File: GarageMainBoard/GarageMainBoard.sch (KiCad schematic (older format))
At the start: 33 parts, among them J1 Conn_01x02, J2 Barrel_Jack, J3 Conn_02x13_Odd_Even, J4 Front_Panel_Connector, J5 RJ45, J6 RJ45, Q1 IRLML6344, Q2 IRLML6344, Q3 IRLML6344, U1 AP1117-33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

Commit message: Main PCB start
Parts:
- BZ1: footprint (none) -> Buzzers_Beepers:BUZZER
- C1: footprint (none) -> Capacitors_THT:CP_Radial_D10.0mm_P2.50mm
- C2, C3, C4, C5: footprint (none) -> Capacitors_SMD:C_0805_HandSoldering
- J1: footprint (none) -> Pin_Headers:Pin_Header_Straight_1x02
- J2: footprint (none) -> Connectors:BARREL_JACK
- J3: footprint (none) -> Pin_Headers:Pin_Header_Straight_2x13
- J4: footprint (none) -> Connectors_JST:JST_PH_B8B-PH-K_08x2.00mm_Straight
- J5, J6: footprint (none) -> KevinLibrary:RJ45_LOW_PROFILE_NO_CUT
- Q1, Q2, Q3: footprint (none) -> TO_SOT_Packages_SMD:SOT-23_Handsoldering
- R1, R10, R11, R12, R13, R14, R15, R2, R3, R4, R5, R6, R7, R8, R9: footprint (none) -> Resistors_SMD:R_0805_HandSoldering
- U2, U3: footprint (none) -> KevinLibrary:SLP1616P6
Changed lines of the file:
@@
 LIBS:contrib
 LIBS:valves
-LIBS:KevinsLib
+LIBS:GarageMainBoard-cache
 EELAYER 25 0
 EELAYER END
@@
 F 0 "J5" H 10350 3600 50  0000 C CNN
 F 1 "RJ45" H 10000 3600 50  0000 C CNN
-F 2 "" H 10150 3100 50  0001 C CNN
+F 2 "KevinLibrary:RJ45_LOW_PROFILE_NO_CUT" H 10150 3100 50  0001 C CNN
 F 3 "" H 10150 3100 50  0001 C CNN
 	1    10150 3100
@@
 F 0 "J6" H 10350 5900 50  0000 C CNN
 F 1 "RJ45" H 10000 5900 50  0000 C CNN
-F 2 "" H 10150 5400 50  0001 C CNN
+F 2 "KevinLibrary:RJ45_LOW_PROFILE_NO_CUT" H 10150 5400 50  0001 C CNN
 F 3 "" H 10150 5400 50  0001 C CNN
 	1    10150 5400
@@
 F 0 "J4" H 2350 6050 50  0000 C CNN
 F 1 "Front_Panel_Connector" H 2350 5150 50  0000 C CNN
-F 2 "" H 2350 5650 50  0001 C CNN
+F 2 "Connectors_JST:JST_PH_B8B-PH-K_08x2.00mm_Straight" H 2350 5650 50  0001 C CNN
 F 3 "" H 2350 5650 50  0001 C CNN
 	1    2350 5650
@@
 F 0 "Q3" H 6200 3000 50  0000 L CNN
 F 1 "IRLML6344" H 6200 2900 50  0000 L CNN
-F 2 "" H 6200 3050 50  0001 C CNN
+F 2 "TO_SOT_Packages_SMD:SOT-23_Handsoldering" H 6200 3050 50  0001 C CNN
 F 3 "" H 6000 2950 50  0001 C CNN
 	1    6000 2950
@@
 F 0 "Q1" H 4400 3000 50  0000 L CNN
 F 1 "IRLML6344" H 4400 2900 50  0000 L CNN
-F 2 "" H 4400 3050 50  0001 C CNN
+F 2 "TO_SOT_Packages_SMD:SOT-23_Handsoldering" H 4400 3050 50  0001 C CNN
 F 3 "" H 4200 2950 50  0001 C CNN
 	1    4200 2950
@@
 F 0 "Q2" H 5550 5550 50  0000 L CNN
 F 1 "IRLML6344" H 5550 5450 50  0000 L CNN
-F 2 "" H 5550 5600 50  0001 C CNN
+F 2 "TO_SOT_Packages_SMD:SOT-23_Handsoldering" H 5550 5600 50  0001 C CNN
 F 3 "" H 5350 5500 50  0001 C CNN
 	1    5350 5500
@@
 F 0 "BZ1" H 5900 5100 50  0000 L CNN
 F 1 "Buzzer" H 5900 5000 50  0000 L CNN
-F 2 "" V 5725 5150 50  0001 C CNN
+F 2 "Buzzers_Beepers:BUZZER" V 5725 5150 50  0001 C CNN
 F 3 "" V 5725 5150 50  0001 C CNN
 	1    5750 5050
@@
 F 0 "R10" V 4930 5500 50  0000 C CNN
 F 1 "100R" V 4850 5500 50  0000 C CNN
-F 2 "" V 4780 5500 50  0001 C CNN
+F 2 "Resistors_SMD:R_0805_HandSoldering" V 4780 5500 50  0001 C CNN
 F 3 "" H 4850 5500 50  0001 C CNN
 	1    4850 5500
@@
 F 0 "R11" V 5180 5850 50  0000 C CNN
 F 1 "100K" V 5100 5850 50  0000 C CNN
-F 2 "" V 5030 5850 50  0001 C CNN
+F 2 "Resistors_SMD:R_0805_HandSoldering" V 5030 5850 50  0001 C CNN
 F 3 "" H 5100 5850 50  0001 C CNN
 	1    5100 5850
@@
 F 0 "R13" V 5530 5050 50  0000 C CNN
 F 1 "1K" V 5450 5050 50  0000 C CNN
-F 2 "" V 5380 5050 50  0001 C CNN
+F 2 "Resistors_SMD:R_0805_HandSoldering" V 5380 5050 50  0001 C CNN
 F 3 "" H 5450 5050 50  0001 C CNN
 	1    5450 5050
@@
 F 0 "J3" H 2300 4550 50  0000 C CNN
 F 1 "Conn_02x13_Odd_Even" H 2300 3150 50  0000 C CNN
-F 2 "" H 2250 3850 50  0001 C CNN
+F 2 "Pin_Headers:Pin_Header_Straight_2x13" H 2250 3850 50  0001 C CNN
 F 3 "" H 2250 3850 50  0001 C CNN
 	1    2250 3850
@@
 F 0 "U3" H 7900 5425 60  0000 C CNN
 F 1 "uClamp3306" H 8700 5450 60  0000 C CNN
-F 2 "" H 8350 5450 60  0001 C CNN
+F 2 "KevinLibrary:SLP1616P6" H 8350 5450 60  0001 C CNN
 F 3 "" H 8350 5450 60  0001 C CNN
 	1    8350 5600
@@
 F 0 "U2" H 7800 3275 60  0000 C CNN
 F 1 "uClamp3306" H 8600 3300 60  0000 C CNN
-F 2 "" H 8250 3300 60  0001 C CNN
+F 2 "KevinLibrary:SLP1616P6" H 8250 3300 60  0001 C CNN
 F 3 "" H 8250 3300 60  0001 C CNN
 	1    8250 3450
@@
 F 0 "R15" V 7680 2350 50  0000 C CNN
 F 1 "1K" V 7600 2350 50  0000 C CNN
-F 2 "" V 7530 2350 50  0001 C CNN
+F 2 "Resistors_SMD:R_0805_HandSoldering" V 7530 2350 50  0001 C CNN
 F 3 "" H 7600 2350 50  0001 C CNN
 	1    7600 2350
@@
 F 0 "C5" H 7275 2450 50  0000 L CNN
 F 1 "100n" H 7275 2250 50  0000 L CNN
-F 2 "" H 7288 2200 50  0001 C CNN
+F 2 "Capacitors_SMD:C_0805_HandSoldering" H 7288 2200 50  0001 C CNN
 F 3 "" H 7250 2350 50  0001 C CNN
 	1    7250 2350
@@
 F 0 "R7" V 2880 4050 50  0000 C CNN
 F 1 "1OOR" V 2800 4050 50  0000 C CNN
-F 2 "" V 2730 4050 50  0001 C CNN
+F 2 "Resistors_SMD:R_0805_HandSoldering" V 2730 4050 50  0001 C CNN
 F 3 "" H 2800 4050 50  0001 C CNN
 	1    2800 4050
@@
 F 0 "R12" V 5480 2950 50  0000 C CNN
 F 1 "100R" V 5400 2950 50  0000 C CNN
-F 2 "" V 5330 2950 50  0001 C CNN
+F 2 "Resistors_SMD:R_0805_HandSoldering" V 5330 2950 50  0001 C CNN
 F 3 "" H 5400 2950 50  0001 C CNN
 	1    5400 2950
@@
 F 0 "R14" V 5780 3200 50  0000 C CNN
 F 1 "100K" V 5700 3200 50  0000 C CNN
-F 2 "" V 5630 3200 50  0001 C CNN
+F 2 "Resistors_SMD:R_0805_HandSoldering" V 5630 3200 50  0001 C CNN
 F 3 "" H 5700 3200 50  0001 C CNN
 	1    5700 3200
@@
 F 0 "R9" V 3980 3250 50  0000 C CNN
 F 1 "100K" V 3900 3250 50  0000 C CNN
-F 2 "" V 3830 3250 50  0001 C CNN
+F 2 "Resistors_SMD:R_0805_HandSoldering" V 3830 3250 50  0001 C CNN
 F 3 "" H 3900 3250 50  0001 C CNN
 	1    3900 3250
@@
 F 0 "R8" V 3680 2950 50  0000 C CNN
 F 1 "100R" V 3600 2950 50  0000 C CNN
-F 2 "" V 3530 2950 50  0001 C CNN
+F 2 "Resistors_SMD:R_0805_HandSoldering" V 3530 2950 50  0001 C CNN
 F 3 "" H 3600 2950 50  0001 C CNN
 	1    3600 2950
@@
 F 0 "C4" H 5225 2600 50  0000 L CNN
 F 1 "100u" H 5225 2400 50  0000 L CNN
-F 2 "" H 5238 2350 50  0001 C CNN
+F 2 "Capacitors_SMD:C_0805_HandSoldering" H 5238 2350 50  0001 C CNN
 F 3 "" H 5200 2500 50  0001 C CNN
 	1    5200 2500
@@
 F 0 "R3" V 1830 3750 50  0000 C CNN
 F 1 "100R" V 1750 3750 50  0000 C CNN
-F 2 "" V 1680 3750 50  0001 C CNN
+F 2 "Resistors_SMD:R_0805_HandSoldering" V 1680 3750 50  0001 C CNN
 F 3 "" H 1750 3750 50  0001 C CNN
 	1    1750 3750
@@
 F 0 "R4" V 1830 3900 50  0000 C CNN
 F 1 "100R" V 1750 3900 50  0000 C CNN
-F 2 "" V 1680 3900 50  0001 C CNN
+F 2 "Resistors_SMD:R_0805_HandSoldering" V 1680 3900 50  0001 C CNN
 F 3 "" H 1750 3900 50  0001 C CNN
 	1    1750 3900
@@
 F 0 "J2" H 1800 2210 50  0000 C CNN
 F 1 "Barrel_Jack" H 1800 1825 50  0000 C CNN
-F 2 "" H 1850 1960 50  0001 C CNN
+F 2 "Connectors:BARREL_JACK" H 1850 1960 50  0001 C CNN
 F 3 "" H 1850 1960 50  0001 C CNN
 	1    1800 2000
@@
 F 0 "C1" H 2425 2100 50  0000 L CNN
 F 1 "CP1" H 2425 1900 50  0000 L CNN
-F 2 "" H 2400 2000 50  0001 C CNN
+F 2 "Capacitors_THT:CP_Radial_D10.0mm_P2.50mm" H 2400 2000 50  0001 C CNN
 F 3 "" H 2400 2000 50  0001 C CNN
 	1    2400 2000
@@
 F 0 "J1" H 1200 1500 50  0000 C CNN
 F 1 "Conn_01x02" H 1200 1200 50  0000 C CNN
-F 2 "" H 1200 1400 50  0001 C CNN
+F 2 "Pin_Headers:Pin_Header_Straight_1x02" H 1200 1400 50  0001 C CNN
 F 3 "" H 1200 1400 50  0001 C CNN
 	1    1200 1400
@@
 F 0 "C2" H 3275 1650 50  0000 L CNN
 F 1 "100n" H 3275 1450 50  0000 L CNN
-F 2 "" H 3288 1400 50  0001 C CNN
+F 2 "Capacitors_SMD:C_0805_HandSoldering" H 3288 1400 50  0001 C CNN
 F 3 "" H 3250 1550 50  0001 C CNN
 	1    3250 1550
@@
 F 0 "C3" H 4325 1650 50  0000 L CNN
 F 1 "10u" H 4325 1450 50  0000 L CNN
-F 2 "" H 4338 1400 50  0001 C CNN
+F 2 "Capacitors_SMD:C_0805_HandSoldering" H 4338 1400 50  0001 C CNN
 F 3 "" H 4300 1550 50  0001 C CNN
 	1    4300 1550
@@
 F 0 "R5" V 1830 4050 50  0000 C CNN
 F 1 "100R" V 1750 4050 50  0000 C CNN
-F 2 "" V 1680 4050 50  0001 C CNN
+F 2 "Resistors_SMD:R_0805_HandSoldering" V 1680 4050 50  0001 C CNN
 F 3 "" H 1750 4050 50  0001 C CNN
 	1    1750 4050
@@
 F 0 "R6" V 1830 4200 50  0000 C CNN
 F 1 "100R" V 1750 4200 50  0000 C CNN
-F 2 "" V 1680 4200 50  0001 C CNN
+F 2 "Resistors_SMD:R_0805_HandSoldering" V 1680 4200 50  0001 C CNN
 F 3 "" H 1750 4200 50  0001 C CNN
 	1    1750 4200
@@
 F 0 "R1" V 1830 3300 50  0000 C CNN
 F 1 "100R" V 1750 3300 50  0000 C CNN
-F 2 "" V 1680 3300 50  0001 C CNN
+F 2 "Resistors_SMD:R_0805_HandSoldering" V 1680 3300 50  0001 C CNN
 F 3 "" H 1750 3300 50  0001 C CNN
 	1    1750 3300
@@
 F 0 "R2" V 1830 3450 50  0000 C CNN
 F 1 "100R" V 1750 3450 50  0000 C CNN
-F 2 "" V 1680 3450 50  0001 C CNN
+F 2 "Resistors_SMD:R_0805_HandSoldering" V 1680 3450 50  0001 C CNN
 F 3 "" H 1750 3450 50  0001 C CNN
 	1    1750 3450

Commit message: Main PCB
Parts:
- added MP1, MP2, MP3, MP4: MOUNTHOLE, KevinLib:TH-M3, symbol MOUNTHOLE
- BZ1: footprint Buzzers_Beepers:BUZZER -> Buzzers_Beepers:Buzzer_12x9.5RM7.6
- C1: value CP1 -> 220u; footprint Capacitors_THT:CP_Radial_D10.0mm_P2.50mm -> Capacitors_THT:CP_Radial_D6.3mm_P2.50mm
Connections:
- wire segments 120 -> 118
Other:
- moved on the sheet: C5, R15
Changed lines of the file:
@@
 LIBS:contrib
 LIBS:valves
+LIBS:KevinsLib
 LIBS:GarageMainBoard-cache
 EELAYER 25 0
@@
 F 0 "BZ1" H 5900 5100 50  0000 L CNN
 F 1 "Buzzer" H 5900 5000 50  0000 L CNN
-F 2 "Buzzers_Beepers:BUZZER" V 5725 5150 50  0001 C CNN
+F 2 "Buzzers_Beepers:Buzzer_12x9.5RM7.6" V 5725 5150 50  0001 C CNN
 F 3 "" V 5725 5150 50  0001 C CNN
 	1    5750 5050
@@
 Text Label 9900 4100 1    60   ~ 0
 HOLD_B
-Text Notes 8150 2400 0    60   ~ 0
+Text Notes 8450 2300 0    60   ~ 0
 Switch/Opener Header\n    Hold Button is connected between pins 2 and 7\n    Hold LED is connected between pins 4 and 5\n    Garage Door Switch is connected between pins 6 and 7
 Text Label 10100 4100 1    60   ~ 0
@@
 L +3.3V #PWR08
 U 1 1 5A5ECDD2
-P 7600 2100
-F 0 "#PWR08" H 7600 1950 50  0001 C CNN
-F 1 "+3.3V" H 7600 2240 50  0000 C CNN
-F 2 "" H 7600 2100 50  0001 C CNN
-F 3 "" H 7600 2100 50  0001 C CNN
-	1    7600 2100
+P 8100 2100
+F 0 "#PWR08" H 8100 1950 50  0001 C CNN
+F 1 "+3.3V" H 8100 2240 50  0000 C CNN
+F 2 "" H 8100 2100 50  0001 C CNN
+F 3 "" H 8100 2100 50  0001 C CNN
+	1    8100 2100
 	1    0    0    -1
 $EndComp
@@
 L R R15
 U 1 1 5A5ECE0B
-P 7600 2350
-F 0 "R15" V 7680 2350 50  0000 C CNN
-F 1 "1K" V 7600 2350 50  0000 C CNN
-F 2 "Resistors_SMD:R_0805_HandSoldering" V 7530 2350 50  0001 C CNN
-F 3 "" H 7600 2350 50  0001 C CNN
-	1    7600 2350
+P 8100 2300
+F 0 "R15" V 8180 2300 50  0000 C CNN
+F 1 "1K" V 8100 2300 50  0000 C CNN
+F 2 "Resistors_SMD:R_0805_HandSoldering" V 8030 2300 50  0001 C CNN
+F 3 "" H 8100 2300 50  0001 C CNN
+	1    8100 2300
 	-1   0    0    1
 $EndComp
-Wire Wire Line
-	7600 2100 7600 2200
-Wire Wire Line
-	7600 2500 7600 3050
-Text Label 7600 3000 1    60   ~ 0
-HOLD_B
+Text Label 7600 3050 1    60   ~ 0
+HOLD_LED_-
 $Comp
 L +3.3V #PWR09
@@
 HOLD_LED_+
 Wire Wire Line
-	8100 3050 8100 2500
+	8100 2450 8100 3050
 Wire Wire Line
 	8400 3050 8400 2500
 Text Label 8100 3050 1    60   ~ 0
-HOLD_LED_-
+HOLD_B
 Text Label 8400 3050 1    60   ~ 0
 DOOR_B
@@
 L +3.3V #PWR011
 U 1 1 5A5EE438
-P 7700 4850
-F 0 "#PWR011" H 7700 4700 50  0001 C CNN
-F 1 "+3.3V" H 7700 4990 50  0000 C CNN
-F 2 "" H 7700 4850 50  0001 C CNN
-F 3 "" H 7700 4850 50  0001 C CNN
-	1    7700 4850
+P 8200 4800
+F 0 "#PWR011" H 8200 4650 50  0001 C CNN
+F 1 "+3.3V" H 8200 4940 50  0000 C CNN
+F 2 "" H 8200 4800 50  0001 C CNN
+F 3 "" H 8200 4800 50  0001 C CNN
+	1    8200 4800
 	1    0    0    -1
 $EndComp
@@
 	7950 5200 7950 4700
 Wire Wire Line
-	8200 5200 8200 4700
+	8200 5200 8200 4800
 Text Label 7950 5200 1    60   ~ 0
 CLOSE_HALL
-Text Label 8200 5150 1    60   ~ 0
+Text Label 7700 5200 1    60   ~ 0
 OPEN_HALL
 Wire Wire Line
-	7700 4850 7700 5200
+	7700 4700 7700 5200
 $Comp
 L C C5
 U 1 1 5A5EE824
-P 7250 2350
-F 0 "C5" H 7275 2450 50  0000 L CNN
-F 1 "100n" H 7275 2250 50  0000 L CNN
-F 2 "Capacitors_SMD:C_0805_HandSoldering" H 7288 2200 50  0001 C CNN
-F 3 "" H 7250 2350 50  0001 C CNN
-	1    7250 2350
-	1    0    0    -1
-$EndComp
-Wire Wire Line
-	7250 2500 7250 2550
-Wire Wire Line
-	7250 2550 7600 2550
-Connection ~ 7600 2550
-Wire Wire Line
-	7250 2200 7250 2150
-Wire Wire Line
-	7250 2150 7600 2150
-Connection ~ 7600 2150
+P 8300 2300
+F 0 "C5" H 8325 2400 50  0000 L CNN
+F 1 "100n" H 8325 2200 50  0000 L CNN
+F 2 "Capacitors_SMD:C_0805_HandSoldering" H 8338 2150 50  0001 C CNN
+F 3 "" H 8300 2300 50  0001 C CNN
+	1    8300 2300
+	1    0    0    -1
+$EndComp
 Wire Wire Line
 	2550 3550 3200 3550
@@
 P 2400 2000
 F 0 "C1" H 2425 2100 50  0000 L CNN
-F 1 "CP1" H 2425 1900 50  0000 L CNN
-F 2 "Capacitors_THT:CP_Radial_D10.0mm_P2.50mm" H 2400 2000 50  0001 C CNN
+F 1 "220u" H 2425 1900 50  0000 L CNN
+F 2 "Capacitors_THT:CP_Radial_D6.3mm_P2.50mm" H 2400 2000 50  0001 C CNN
 F 3 "" H 2400 2000 50  0001 C CNN
 	1    2400 2000
@@
 	3650 2000 3650 1750
 Connection ~ 3650 1750
+Wire Wire Line
+	8100 2100 8100 2150
+Wire Wire Line
+	8300 2450 8100 2450
+Wire Wire Line
+	8100 2150 8300 2150
+Wire Wire Line
+	7600 2400 7600 3050
+$Comp
+L MOUNTHOLE MP1
+U 1 1 5A7A9A16
+P 6000 1400
+F 0 "MP1" H 6000 1250 60  0000 C CNN
+F 1 "MOUNTHOLE" H 6000 1550 60  0000 C CNN
+F 2 "KevinLib:TH-M3" H 6000 1400 60  0001 C CNN
+F 3 "" H 6000 1400 60  0001 C CNN
+	1    6000 1400
+	1    0    0    -1
+$EndComp
+$Comp
+L MOUNTHOLE MP2
+U 1 1 5A7A9AB9
+P 6600 1400
+F 0 "MP2" H 6600 1250 60  0000 C CNN
+F 1 "MOUNTHOLE" H 6600 1550 60  0000 C CNN
+F 2 "KevinLib:TH-M3" H 6600 1400 60  0001 C CNN
+F 3 "" H 6600 1400 60  0001 C CNN
+	1    6600 1400
+	1    0    0    -1
+$EndComp
+$Comp
+L MOUNTHOLE MP3
+U 1 1 5A7A9B7D
+P 7150 1400
+F 0 "MP3" H 7150 1250 60  0000 C CNN
+F 1 "MOUNTHOLE" H 7150 1550 60  0000 C CNN
+F 2 "KevinLib:TH-M3" H 7150 1400 60  0001 C CNN
+F 3 "" H 7150 1400 60  0001 C CNN
+	1    7150 1400
+	1    0    0    -1
+$EndComp
+$Comp
+L MOUNTHOLE MP4
+U 1 1 5A7A9C0F
+P 7700 1400
+F 0 "MP4" H 7700 1250 60  0000 C CNN
+F 1 "MOUNTHOLE" H 7700 1550 60  0000 C CNN
+F 2 "KevinLib:TH-M3" H 7700 1400 60  0001 C CNN
+F 3 "" H 7700 1400 60  0001 C CNN
+	1    7700 1400
+	1    0    0    -1
+$EndComp
 $EndSCHEMATC

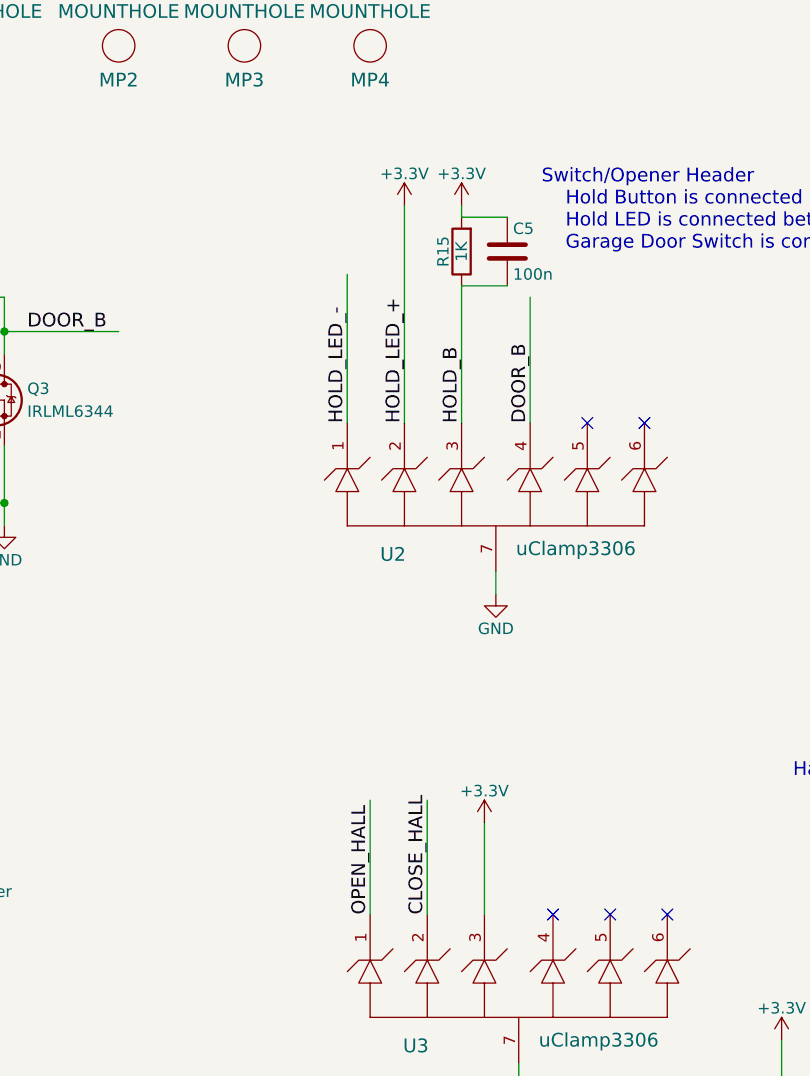
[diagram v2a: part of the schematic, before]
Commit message: Flip Main PCB
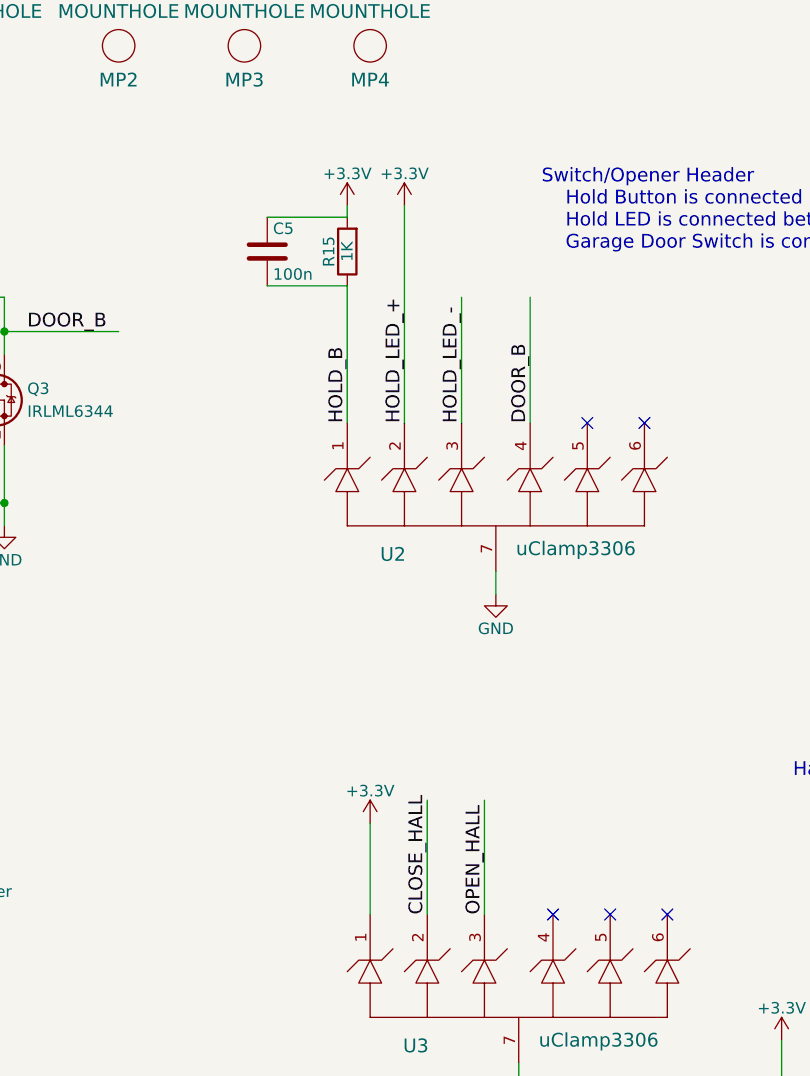
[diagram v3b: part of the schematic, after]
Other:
- moved on the sheet: C5, R15
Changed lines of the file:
@@
 LIBS:contrib
 LIBS:valves
-LIBS:KevinsLib
 LIBS:GarageMainBoard-cache
 EELAYER 25 0
@@
 L +3.3V #PWR08
 U 1 1 5A5ECDD2
-P 8100 2100
-F 0 "#PWR08" H 8100 1950 50  0001 C CNN
-F 1 "+3.3V" H 8100 2240 50  0000 C CNN
-F 2 "" H 8100 2100 50  0001 C CNN
-F 3 "" H 8100 2100 50  0001 C CNN
-	1    8100 2100
+P 7600 2100
+F 0 "#PWR08" H 7600 1950 50  0001 C CNN
+F 1 "+3.3V" H 7600 2240 50  0000 C CNN
+F 2 "" H 7600 2100 50  0001 C CNN
+F 3 "" H 7600 2100 50  0001 C CNN
+	1    7600 2100
 	1    0    0    -1
 $EndComp
@@
 L R R15
 U 1 1 5A5ECE0B
-P 8100 2300
-F 0 "R15" V 8180 2300 50  0000 C CNN
-F 1 "1K" V 8100 2300 50  0000 C CNN
-F 2 "Resistors_SMD:R_0805_HandSoldering" V 8030 2300 50  0001 C CNN
-F 3 "" H 8100 2300 50  0001 C CNN
-	1    8100 2300
+P 7600 2300
+F 0 "R15" V 7680 2300 50  0000 C CNN
+F 1 "1K" V 7600 2300 50  0000 C CNN
+F 2 "Resistors_SMD:R_0805_HandSoldering" V 7530 2300 50  0001 C CNN
+F 3 "" H 7600 2300 50  0001 C CNN
+	1    7600 2300
 	-1   0    0    1
 $EndComp
-Text Label 7600 3050 1    60   ~ 0
+Text Label 8100 3050 1    60   ~ 0
 HOLD_LED_-
 $Comp
@@
 HOLD_LED_+
 Wire Wire Line
-	8100 2450 8100 3050
+	7600 2450 7600 3050
 Wire Wire Line
 	8400 3050 8400 2500
-Text Label 8100 3050 1    60   ~ 0
+Text Label 7600 3050 1    60   ~ 0
 HOLD_B
 Text Label 8400 3050 1    60   ~ 0
@@
 L +3.3V #PWR011
 U 1 1 5A5EE438
-P 8200 4800
-F 0 "#PWR011" H 8200 4650 50  0001 C CNN
-F 1 "+3.3V" H 8200 4940 50  0000 C CNN
-F 2 "" H 8200 4800 50  0001 C CNN
-F 3 "" H 8200 4800 50  0001 C CNN
-	1    8200 4800
+P 7700 4800
+F 0 "#PWR011" H 7700 4650 50  0001 C CNN
+F 1 "+3.3V" H 7700 4940 50  0000 C CNN
+F 2 "" H 7700 4800 50  0001 C CNN
+F 3 "" H 7700 4800 50  0001 C CNN
+	1    7700 4800
 	1    0    0    -1
 $EndComp
@@
 	7950 5200 7950 4700
 Wire Wire Line
-	8200 5200 8200 4800
+	8200 5200 8200 4700
 Text Label 7950 5200 1    60   ~ 0
 CLOSE_HALL
-Text Label 7700 5200 1    60   ~ 0
+Text Label 8200 5200 1    60   ~ 0
 OPEN_HALL
 Wire Wire Line
-	7700 4700 7700 5200
+	7700 4800 7700 5200
 $Comp
 L C C5
 U 1 1 5A5EE824
-P 8300 2300
-F 0 "C5" H 8325 2400 50  0000 L CNN
-F 1 "100n" H 8325 2200 50  0000 L CNN
-F 2 "Capacitors_SMD:C_0805_HandSoldering" H 8338 2150 50  0001 C CNN
-F 3 "" H 8300 2300 50  0001 C CNN
-	1    8300 2300
+P 7250 2300
+F 0 "C5" H 7275 2400 50  0000 L CNN
+F 1 "100n" H 7275 2200 50  0000 L CNN
+F 2 "Capacitors_SMD:C_0805_HandSoldering" H 7288 2150 50  0001 C CNN
+F 3 "" H 7250 2300 50  0001 C CNN
+	1    7250 2300
 	1    0    0    -1
 $EndComp
@@
 Connection ~ 3650 1750
 Wire Wire Line
-	8100 2100 8100 2150
-Wire Wire Line
-	8300 2450 8100 2450
-Wire Wire Line
-	8100 2150 8300 2150
-Wire Wire Line
-	7600 2400 7600 3050
+	7600 2100 7600 2150
+Wire Wire Line
+	7250 2450 7600 2450
+Wire Wire Line
+	7600 2150 7250 2150
 $Comp
 L MOUNTHOLE MP1
@@
 	1    0    0    -1
 $EndComp
+Wire Wire Line
+	8100 3050 8100 2500
 $EndSCHEMATC

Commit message: Main Board V2
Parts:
- removed R7: 1OOR, Resistors_SMD:R_0805_HandSoldering, symbol R
- removed U1: AP1117-33, TO_SOT_Packages_SMD:SOT-223-3Lead_TabPin2, symbol AP1117-33
- removed U2, U3: uClamp3306, KevinLibrary:SLP1616P6, symbol uClamp3306
- added J7: 5V Jumper, Pin_Headers:Pin_Header_Straight_1x02, symbol Conn_01x02
- added U1: MC74HC365A, MODULE, symbol MC74HC365A
- added U2: CPDV5-3V3UP, symbol CPDV5-3V3UP
- added U3: CPDV5-3V3UP, TO_SOT_Packages_SMD:SOT-353_SC-70-5_Handsoldering, symbol CPDV5-3V3UP
- added U4: TVS 20VDC, Diodes_SMD:D_SMB, symbol TVS
- added U5: MC74VHC1GT50, MODULE, symbol MC74VHC1GT50
- C3: value 10u -> 100n
- C4: value 100u -> 1uF
- R5: value 100R -> 10K
- R6: value 100R -> 100
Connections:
- net labels added: ENABLE_1, ENABLE_2, G_DOOR_X, HOLD_LED, HOLD_LED_X, LIGHT_X, MOSI_X, PIEZO_X
- net labels removed: HOLD_LED_-
- wire segments 118 -> 153
- no-connect marks 24 -> 19
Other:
- moved on the sheet: C1, J2
